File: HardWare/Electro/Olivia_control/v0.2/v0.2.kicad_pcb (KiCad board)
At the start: 2 copper layers, 90 x 100 mm, 47 parts, among them J1 PROG, J10 Motor_B, J11 I2C, J12 DAC, J13 UART2, J15 TRIAC_220VAC, J17 In12V, J2 Input1, J3 Input2, J4 Input3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

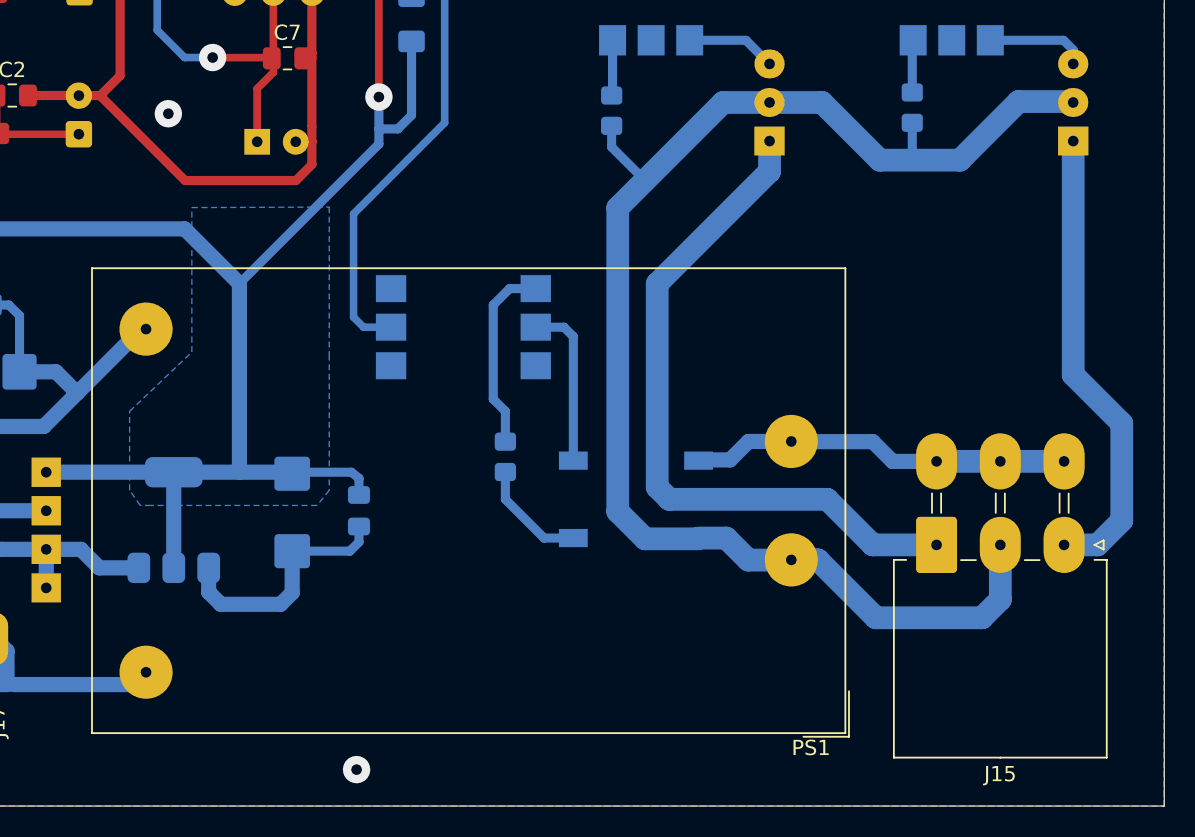
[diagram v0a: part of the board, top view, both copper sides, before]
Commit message: Reemplazo de Conector 220V por borneras 7,62mm.
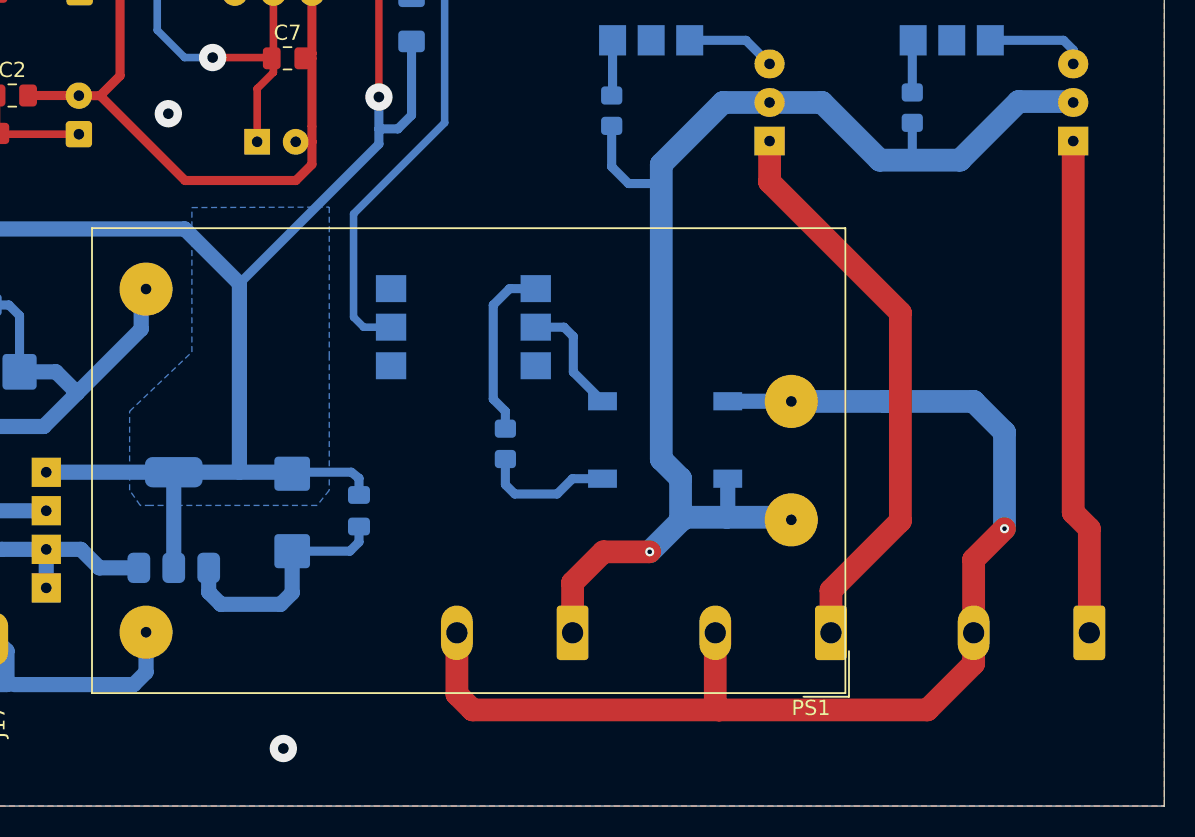
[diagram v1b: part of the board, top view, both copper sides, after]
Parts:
- added J14: TRIAC OUT_A, Connector_Phoenix_GMSTB:PhoenixContact_GMSTBA_2,5_2-G-7,62_1x02_P7.62mm_Horizontal, B.Cu at (98.0, 148.6)
- added J16: 220V IN, Connector_Phoenix_GMSTB:PhoenixContact_GMSTBA_2,5_2-G-7,62_1x02_P7.62mm_Horizontal, B.Cu at (81.0, 148.6)
- J15: value TRIAC_220VAC -> TRIAC OUT_B; footprint lib:Molex_Mini-Fit_Jr_5569-06A2_2x03_P4.20mm_Horizontal_NoHoles -> Connector_Phoenix_GMSTB:PhoenixContact_GMSTBA_2,5_2-G-7,62_1x02_P7.62mm_Horizontal; moved to B.Cu
- moved J15 6.02 mm to (115.1, 148.6)
- moved BR1 4.36 mm to (87.1, 135.9)
- moved PS1 2.64 mm to (95.4, 141.2)
- moved R11 0.86 mm to (76.6, 136.1)
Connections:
- J15 pad 2: /FASE -> /NEUTRO
- Q1 pad 1: Net-(J15-Pin_1) -> Net-(J14-Pin_1)
- Q2 pad 1: Net-(J15-Pin_3) -> Net-(J15-Pin_1)
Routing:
- net /NEUTRO: track 25.1 -> 79.4 mm, vias 0 -> 1
- net Net-(J14-Pin_1): track 0.00 -> 37.9 mm
- net Net-(J15-Pin_3): track 30.8 -> 0.00 mm
- net Net-(J15-Pin_1): track 45.8 -> 32.8 mm
- net /FASE: track 95.4 -> 87.0 mm, vias 0 -> 1
- net Net-(BR1-Pad-): track 10.9 -> 7.79 mm
- net GND: track 477.8 -> 480.4 mm
- net Net-(PS1-+Vout): track 53.0 -> 55.5 mm
- net /380V: track 7.33 -> 8.75 mm
- net Net-(R11-Pad2): track 12.6 -> 11.7 mm

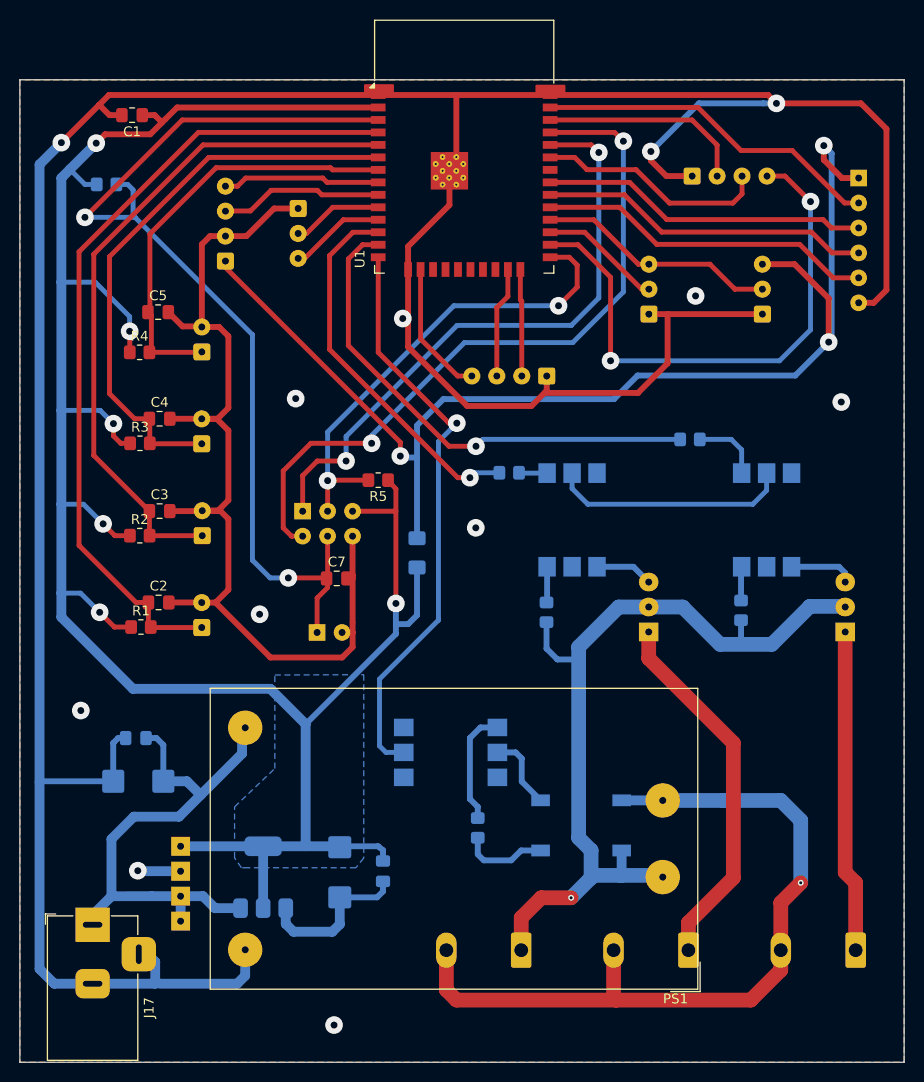
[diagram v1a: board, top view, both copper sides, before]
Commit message: Cambio de medidas de huecos y pads para llevar a proceso de fabricación industrial. La version original tiene margenes de tolerancia adaptados a las impresiciones de la fabricación manual.
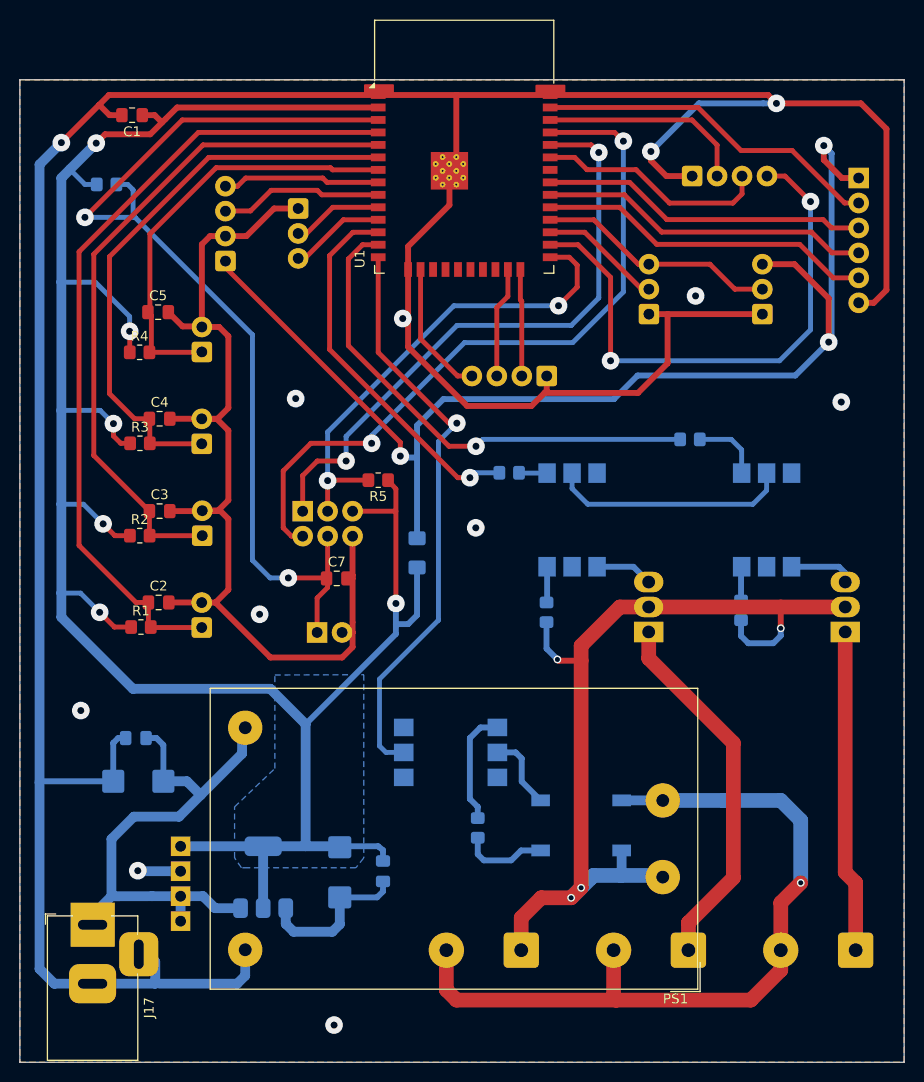
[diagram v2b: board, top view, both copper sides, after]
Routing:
- net /FASE: track 87.0 -> 92.6 mm, vias 1 -> 4
